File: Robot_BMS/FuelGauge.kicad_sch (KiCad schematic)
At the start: 8 parts, among them IC1 BQ34Z100PWR-R2

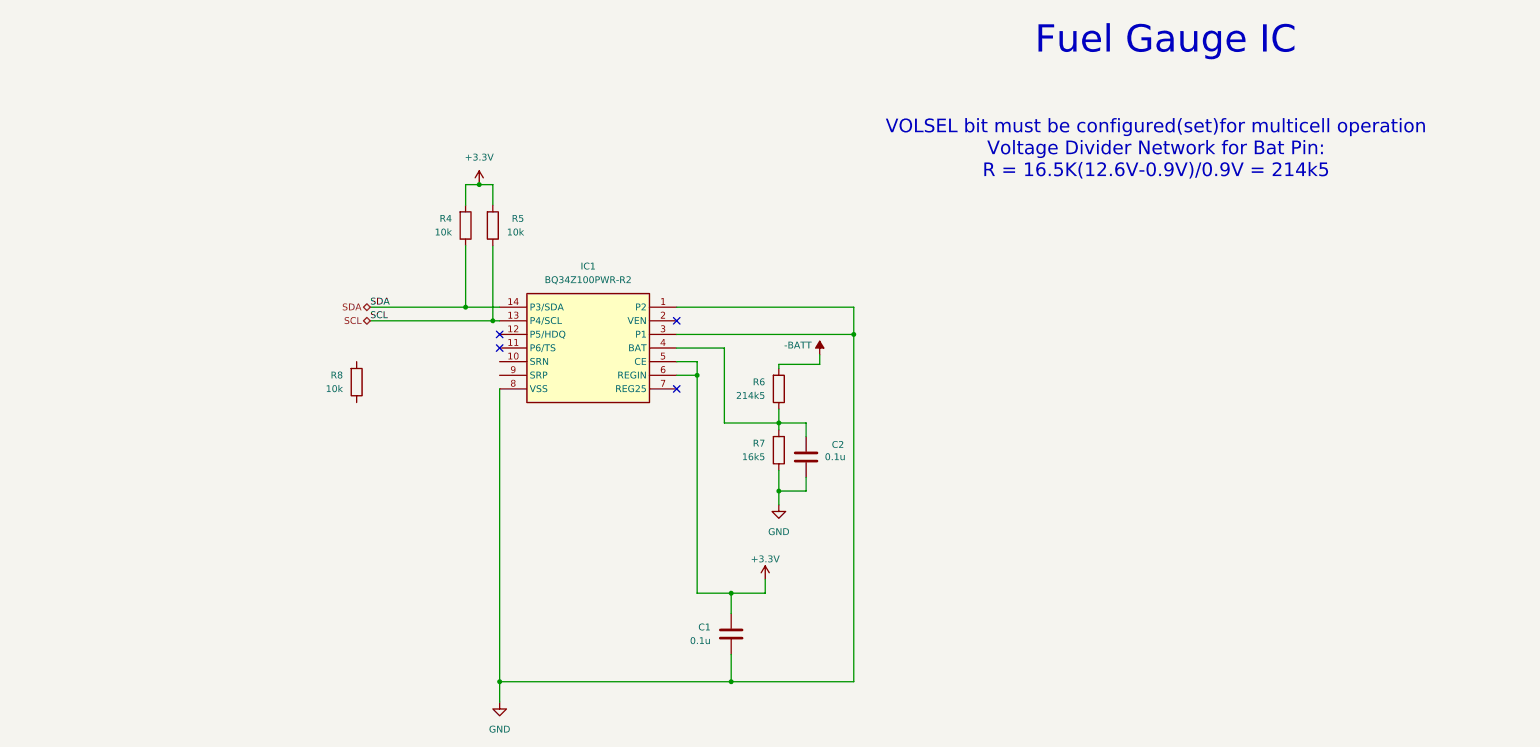
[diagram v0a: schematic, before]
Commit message: DC power supply added via dc Barrel jack
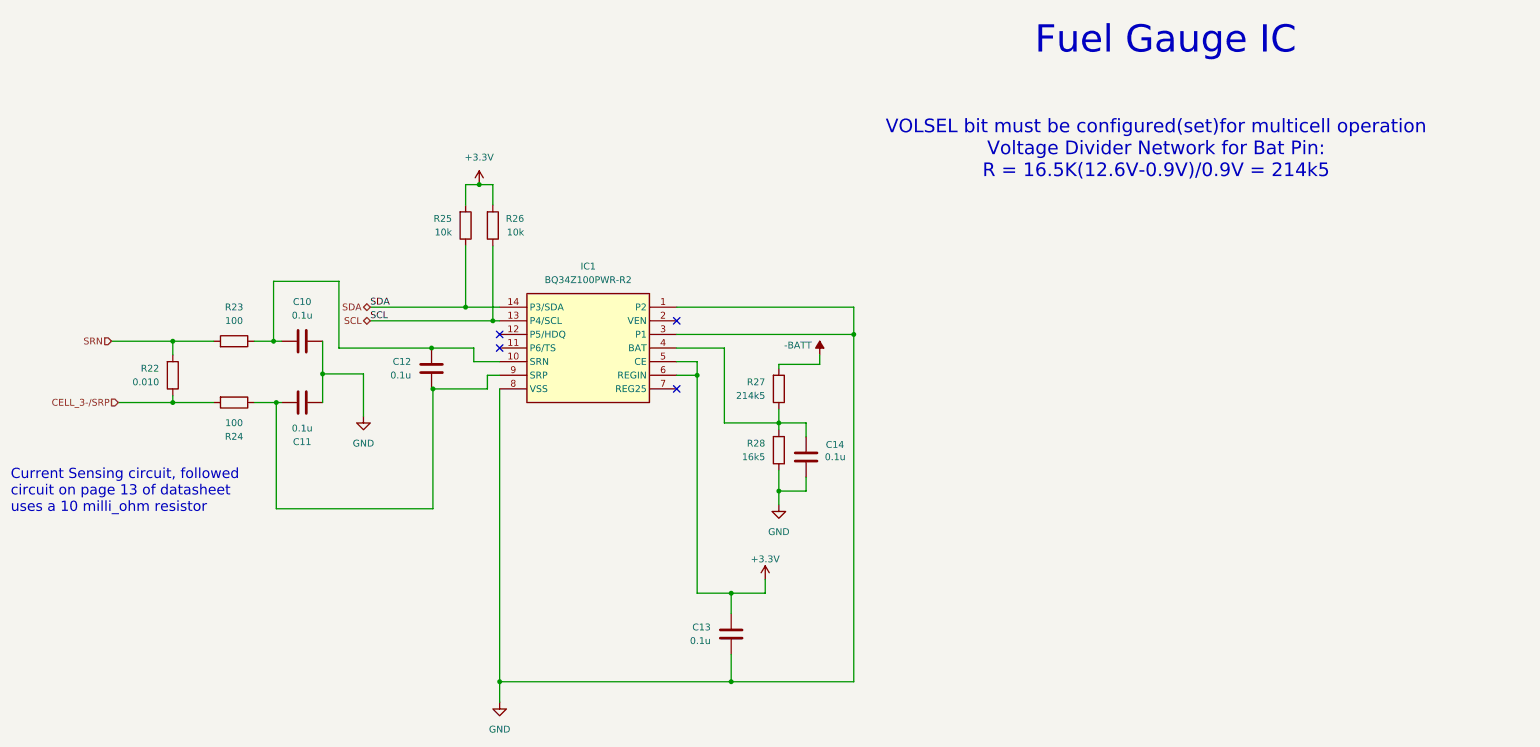
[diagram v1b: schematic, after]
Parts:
- added C10, C11, C12: 0.1u, symbol Device:C
- added R23, R24: 100, symbol Device:R
- R22: renamed from R8; value 10k -> 0.010
- renumbered C1 to C13, C2 to C14, R4 to R25, R5 to R26, R6 to R27, R7 to R28
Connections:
- net GND: now also C10.2, C11.2
- net at IC1.10 (SRN): now also C10.1, C12.1, R23.1
- net at IC1.9 (SRP): now also C11.1, C12.2, R24.1
- net CELL_3-/SRP: now reaches R22.1
- net CELL_3-/SRP: now also R24.2
- net SRN: now reaches R22.2
- net SRN: now also R23.2
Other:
- note added: "Current Sensing circuit, followed circuit on page 13 of datasheet uses a 10 milli_ohm resistor"
- moved on the sheet: R22

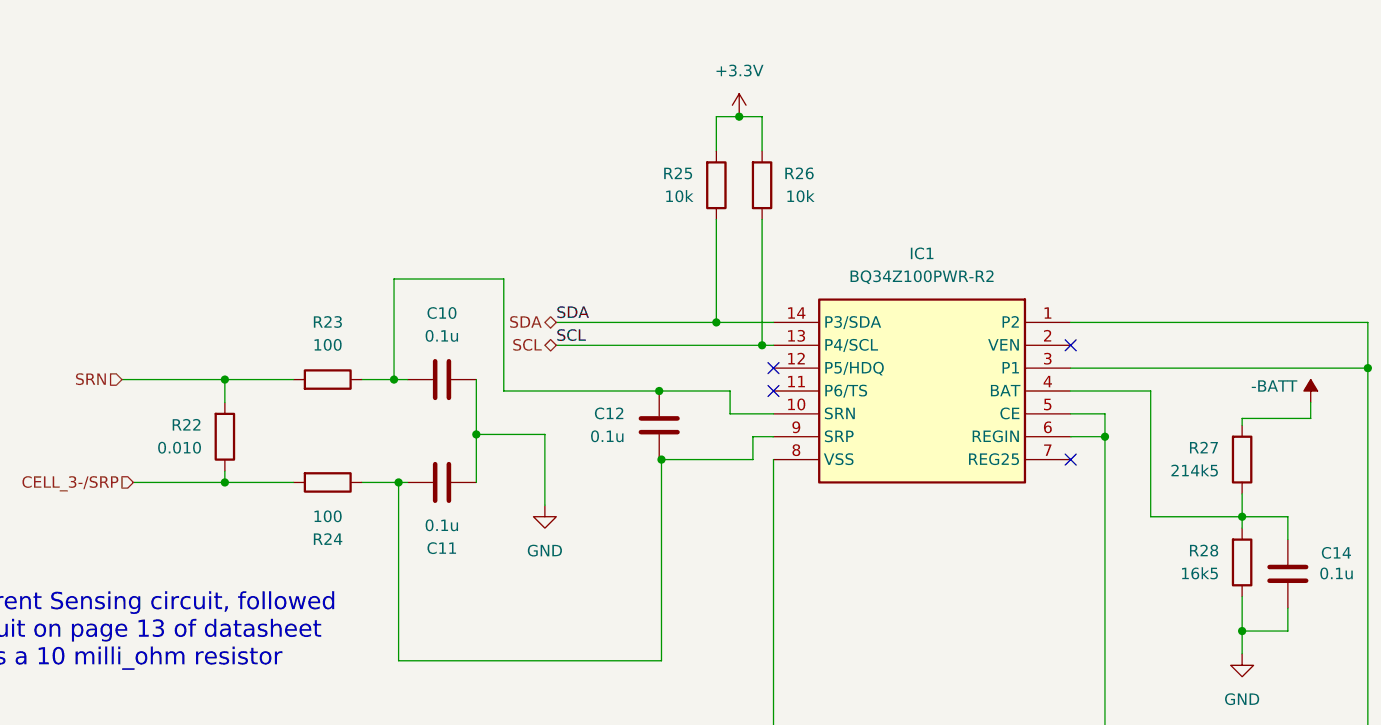
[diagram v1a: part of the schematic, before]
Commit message: implementing sepic converter for Solar power input
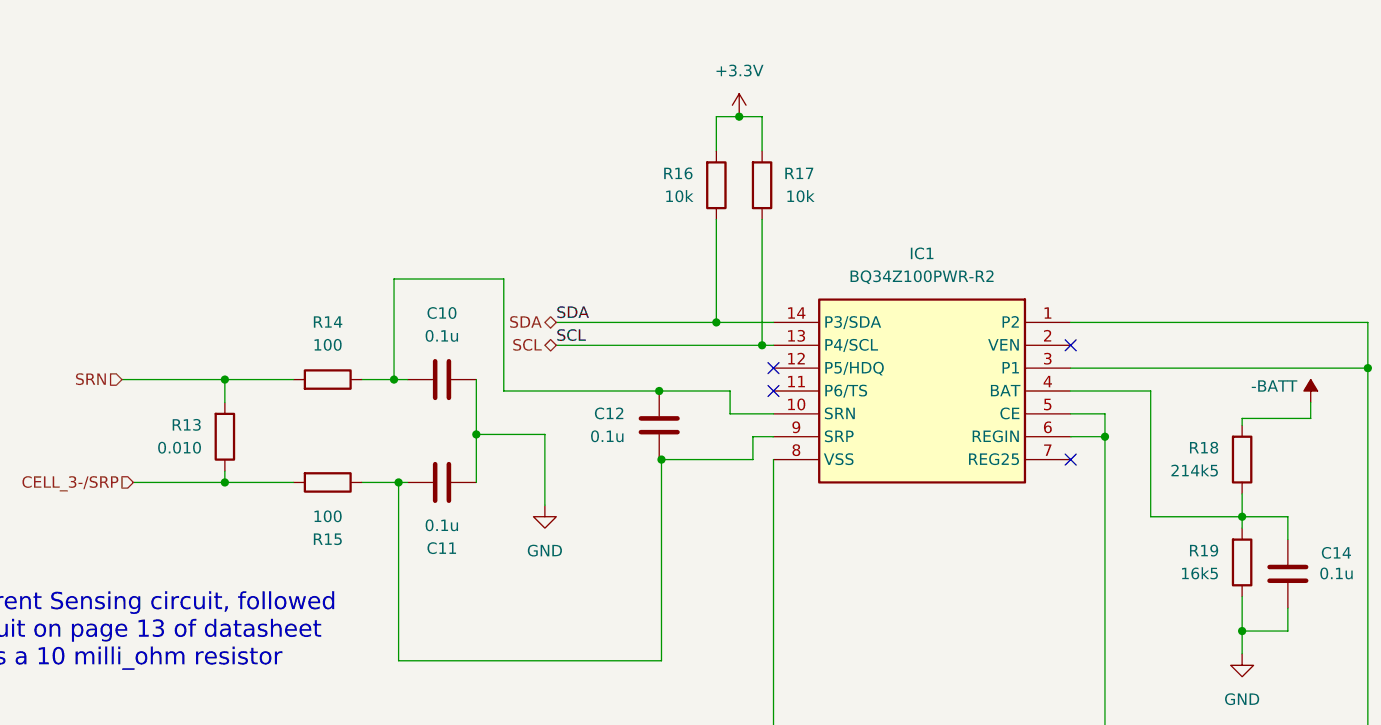
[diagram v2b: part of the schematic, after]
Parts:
- renumbered R22 to R13, R23 to R14, R24 to R15, R25 to R16, R26 to R17, R27 to R18, R28 to R19
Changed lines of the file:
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@@
 		(dnp no)
 		(fields_autoplaced yes)
-		(property "Reference" "R22"
+		(property "Reference" "R13"
 			(at 40.64 86.3599 0)
 			(effects
@@
 			(project "Robot_BMS"
 				(path "/72551b1c-3d40-4199-8911-e5b015f4abec/ddc79d9c-dbaa-4c26-8116-aed3dbdb681b"
-					(reference "R22")
+					(reference "R13")
 					(unit 1)
 				)
@@
 		(on_board yes)
 		(dnp no)
-		(property "Reference" "R26"
+		(property "Reference" "R17"
 			(at 108.712 58.42 0)
 			(effects
@@
 			(project "Robot_BMS"
 				(path "/72551b1c-3d40-4199-8911-e5b015f4abec/ddc79d9c-dbaa-4c26-8116-aed3dbdb681b"
-					(reference "R26")
+					(reference "R17")
 					(unit 1)
 				)
@@
 		(dnp no)
 		(fields_autoplaced yes)
-		(property "Reference" "R23"
+		(property "Reference" "R14"
 			(at 54.61 74.93 90)
 			(effects
@@
 			(project "Robot_BMS"
 				(path "/72551b1c-3d40-4199-8911-e5b015f4abec/ddc79d9c-dbaa-4c26-8116-aed3dbdb681b"
-					(reference "R23")
+					(reference "R14")
 					(unit 1)
 				)
@@
 		(dnp no)
 		(fields_autoplaced yes)
-		(property "Reference" "R27"
+		(property "Reference" "R18"
 			(at 153.67 88.8999 0)
 			(effects
@@
 			(project "Robot_BMS"
 				(path "/72551b1c-3d40-4199-8911-e5b015f4abec/ddc79d9c-dbaa-4c26-8116-aed3dbdb681b"
-					(reference "R27")
+					(reference "R18")
 					(unit 1)
 				)
@@
 		(dnp no)
 		(fields_autoplaced yes)
-		(property "Reference" "R28"
+		(property "Reference" "R19"
 			(at 153.67 100.3299 0)
 			(effects
@@
 			(project "Robot_BMS"
 				(path "/72551b1c-3d40-4199-8911-e5b015f4abec/ddc79d9c-dbaa-4c26-8116-aed3dbdb681b"
-					(reference "R28")
+					(reference "R19")
 					(unit 1)
 				)
@@
 		(on_board yes)
 		(dnp no)
-		(property "Reference" "R24"
+		(property "Reference" "R15"
 			(at 54.61 99.06 90)
 			(effects
@@
 			(project "Robot_BMS"
 				(path "/72551b1c-3d40-4199-8911-e5b015f4abec/ddc79d9c-dbaa-4c26-8116-aed3dbdb681b"
-					(reference "R24")
+					(reference "R15")
 					(unit 1)
 				)
@@
 		(dnp no)
 		(fields_autoplaced yes)
-		(property "Reference" "R25"
+		(property "Reference" "R16"
 			(at 95.25 58.4199 0)
 			(effects
@@
 			(project "Robot_BMS"
 				(path "/72551b1c-3d40-4199-8911-e5b015f4abec/ddc79d9c-dbaa-4c26-8116-aed3dbdb681b"
-					(reference "R25")
-					(unit 1)
-				)
+					(reference "R16")
+					(unit 1)
+				)

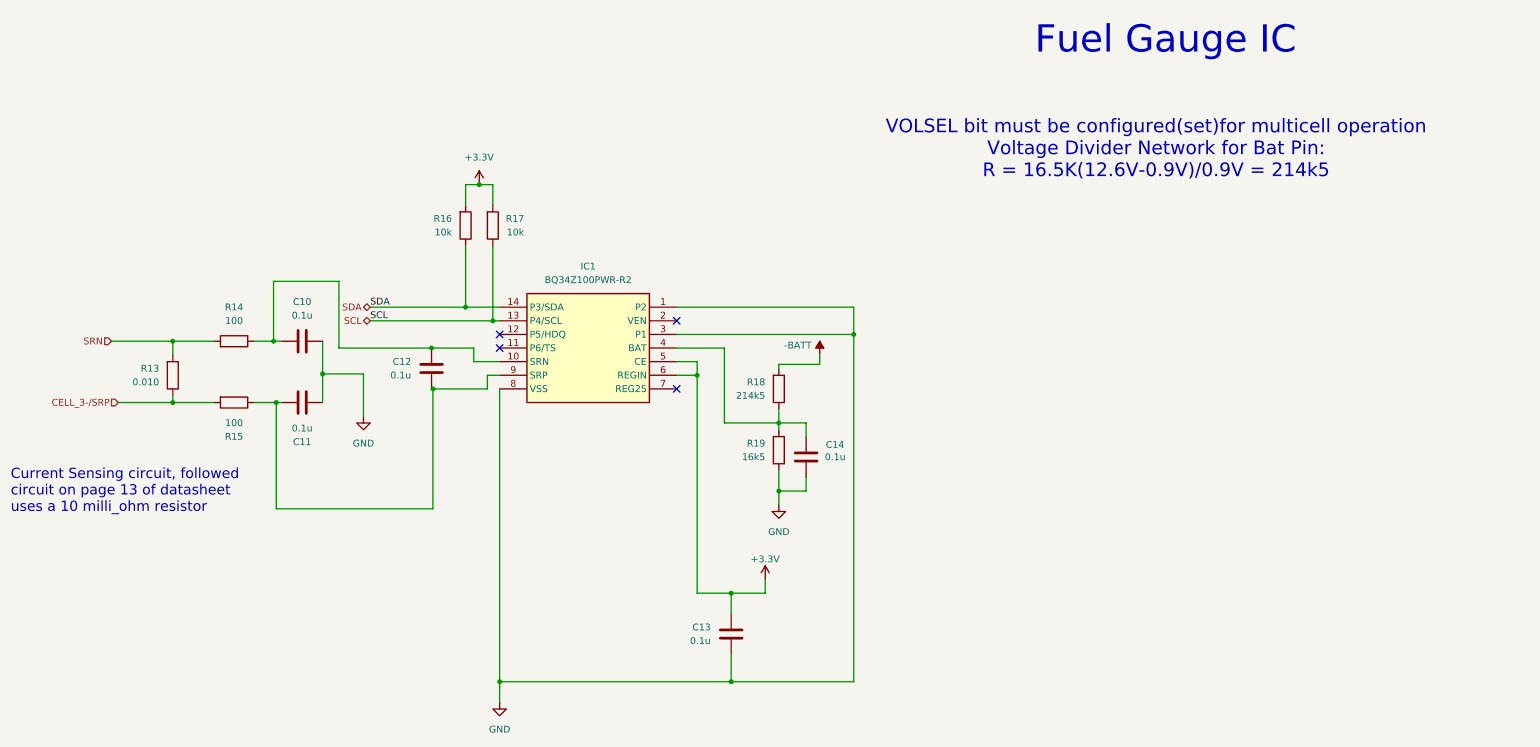
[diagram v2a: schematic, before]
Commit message: solar charger set to 15V
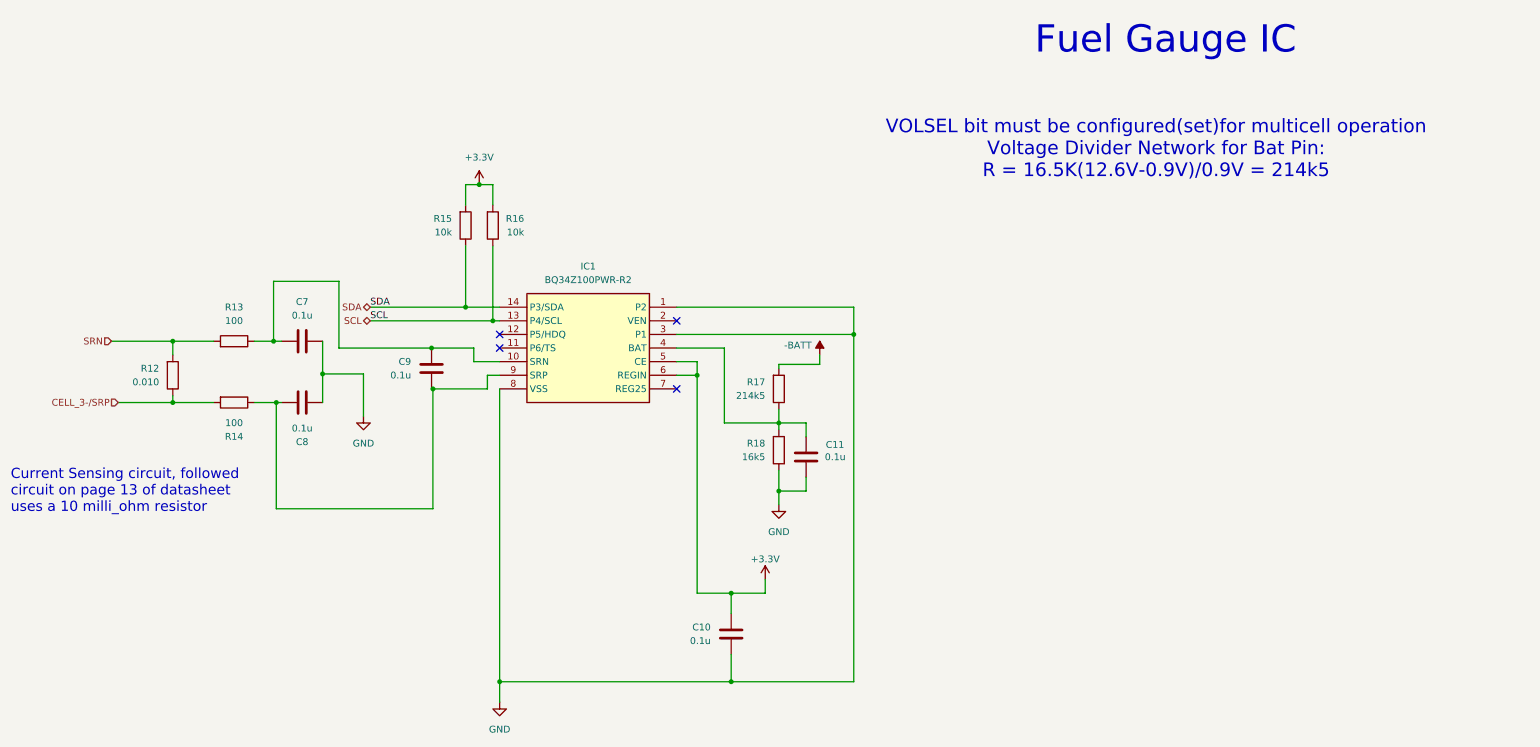
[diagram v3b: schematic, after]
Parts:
- renumbered C13 to C10, C14 to C11, C10 to C7, C11 to C8, C12 to C9, R13 to R12, R14 to R13, R15 to R14, R16 to R15, R17 to R16, R18 to R17, R19 to R18
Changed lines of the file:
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@@
 		(on_board yes)
 		(dnp no)
-		(property "Reference" "#PWR06"
+		(property "Reference" "#PWR010"
 			(at 153.67 129.54 0)
 			(effects
@@
 			(project "Robot_BMS"
 				(path "/72551b1c-3d40-4199-8911-e5b015f4abec/ddc79d9c-dbaa-4c26-8116-aed3dbdb681b"
-					(reference "#PWR06")
+					(reference "#PWR010")
 					(unit 1)
 				)
@@
 		(on_board yes)
 		(dnp no)
-		(property "Reference" "#PWR08"
+		(property "Reference" "#PWR012"
 			(at 163.83 87.63 0)
 			(effects
@@
 			(project "Robot_BMS"
 				(path "/72551b1c-3d40-4199-8911-e5b015f4abec/ddc79d9c-dbaa-4c26-8116-aed3dbdb681b"
-					(reference "#PWR08")
+					(reference "#PWR012")
 					(unit 1)
 				)
@@
 		(dnp no)
 		(fields_autoplaced yes)
-		(property "Reference" "#PWR07"
+		(property "Reference" "#PWR011"
 			(at 156.21 118.11 0)
 			(effects
@@
 			(project "Robot_BMS"
 				(path "/72551b1c-3d40-4199-8911-e5b015f4abec/ddc79d9c-dbaa-4c26-8116-aed3dbdb681b"
-					(reference "#PWR07")
+					(reference "#PWR011")
 					(unit 1)
 				)
@@
 		(dnp no)
 		(fields_autoplaced yes)
-		(property "Reference" "R13"
+		(property "Reference" "R12"
 			(at 40.64 86.3599 0)
 			(effects
@@
 			(project "Robot_BMS"
 				(path "/72551b1c-3d40-4199-8911-e5b015f4abec/ddc79d9c-dbaa-4c26-8116-aed3dbdb681b"
-					(reference "R13")
+					(reference "R12")
 					(unit 1)
 				)
@@
 		(on_board yes)
 		(dnp no)
-		(property "Reference" "R17"
+		(property "Reference" "R16"
 			(at 108.712 58.42 0)
 			(effects
@@
 			(project "Robot_BMS"
 				(path "/72551b1c-3d40-4199-8911-e5b015f4abec/ddc79d9c-dbaa-4c26-8116-aed3dbdb681b"
-					(reference "R17")
+					(reference "R16")
 					(unit 1)
 				)
@@
 		(dnp no)
 		(fields_autoplaced yes)
-		(property "Reference" "#PWR05"
+		(property "Reference" "#PWR09"
 			(at 104.14 154.94 0)
 			(effects
@@
 			(project "Robot_BMS"
 				(path "/72551b1c-3d40-4199-8911-e5b015f4abec/ddc79d9c-dbaa-4c26-8116-aed3dbdb681b"
-					(reference "#PWR05")
+					(reference "#PWR09")
 					(unit 1)
 				)
@@
 		(dnp no)
 		(fields_autoplaced yes)
-		(property "Reference" "C13"
+		(property "Reference" "C10"
 			(at 143.51 134.6199 0)
 			(effects
@@
 			(project "Robot_BMS"
 				(path "/72551b1c-3d40-4199-8911-e5b015f4abec/ddc79d9c-dbaa-4c26-8116-aed3dbdb681b"
-					(reference "C13")
+					(reference "C10")
 					(unit 1)
 				)
@@
 		(dnp no)
 		(fields_autoplaced yes)
-		(property "Reference" "C10"
+		(property "Reference" "C7"
 			(at 67.31 73.9319 90)
 			(effects
@@
 			(project "Robot_BMS"
 				(path "/72551b1c-3d40-4199-8911-e5b015f4abec/ddc79d9c-dbaa-4c26-8116-aed3dbdb681b"
-					(reference "C10")
+					(reference "C7")
 					(unit 1)
 				)
@@
 		(dnp no)
 		(fields_autoplaced yes)
-		(property "Reference" "#PWR04"
+		(property "Reference" "#PWR08"
 			(at 100.33 55.88 0)
 			(effects
@@
 			(project "Robot_BMS"
 				(path "/72551b1c-3d40-4199-8911-e5b015f4abec/ddc79d9c-dbaa-4c26-8116-aed3dbdb681b"
-					(reference "#PWR04")
+					(reference "#PWR08")
 					(unit 1)
 				)
@@
 		(on_board yes)
 		(dnp no)
-		(property "Reference" "C14"
+		(property "Reference" "C11"
 			(at 168.402 100.584 0)
 			(effects
@@
 			(project "Robot_BMS"
 				(path "/72551b1c-3d40-4199-8911-e5b015f4abec/ddc79d9c-dbaa-4c26-8116-aed3dbdb681b"
-					(reference "C14")
+					(reference "C11")
 					(unit 1)
 				)
@@
 		(dnp no)
 		(fields_autoplaced yes)
-		(property "Reference" "#PWR03"
+		(property "Reference" "#PWR07"
 			(at 78.74 101.6 0)
 			(effects
@@
 			(project "Robot_BMS"
 				(path "/72551b1c-3d40-4199-8911-e5b015f4abec/ddc79d9c-dbaa-4c26-8116-aed3dbdb681b"
-					(reference "#PWR03")
+					(reference "#PWR07")
 					(unit 1)
 				)
@@
 		(dnp no)
 		(fields_autoplaced yes)
-		(property "Reference" "R14"
+		(property "Reference" "R13"
 			(at 54.61 74.93 90)
 			(effects
@@
 			(project "Robot_BMS"
 				(path "/72551b1c-3d40-4199-8911-e5b015f4abec/ddc79d9c-dbaa-4c26-8116-aed3dbdb681b"
-					(reference "R14")
+					(reference "R13")
 					(unit 1)
 				)
@@
 		(dnp no)
 		(fields_autoplaced yes)
-		(property "Reference" "R18"
+		(property "Reference" "R17"
 			(at 153.67 88.8999 0)
 			(effects
@@
 			(project "Robot_BMS"
 				(path "/72551b1c-3d40-4199-8911-e5b015f4abec/ddc79d9c-dbaa-4c26-8116-aed3dbdb681b"
-					(reference "R18")
+					(reference "R17")
 					(unit 1)
 				)
@@
 		(dnp no)
 		(fields_autoplaced yes)
-		(property "Reference" "R19"
+		(property "Reference" "R18"
 			(at 153.67 100.3299 0)
 			(effects
@@
 			(project "Robot_BMS"
 				(path "/72551b1c-3d40-4199-8911-e5b015f4abec/ddc79d9c-dbaa-4c26-8116-aed3dbdb681b"
-					(reference "R19")
+					(reference "R18")
 					(unit 1)
 				)
@@
 		(dnp no)
 		(fields_autoplaced yes)
-		(property "Reference" "C12"
+		(property "Reference" "C9"
 			(at 87.63 85.0899 0)
 			(effects
@@
 			(project "Robot_BMS"
 				(path "/72551b1c-3d40-4199-8911-e5b015f4abec/ddc79d9c-dbaa-4c26-8116-aed3dbdb681b"
-					(reference "C12")
+					(reference "C9")
 					(unit 1)
 				)
@@
 		(on_board yes)
 		(dnp no)
-		(property "Reference" "R15"
+		(property "Reference" "R14"
 			(at 54.61 99.06 90)
 			(effects
@@
 			(project "Robot_BMS"
 				(path "/72551b1c-3d40-4199-8911-e5b015f4abec/ddc79d9c-dbaa-4c26-8116-aed3dbdb681b"
-					(reference "R15")
+					(reference "R14")
 					(unit 1)
 				)
@@
 		(dnp no)
 		(fields_autoplaced yes)
-		(property "Reference" "R16"
+		(property "Reference" "R15"
 			(at 95.25 58.4199 0)
 			(effects
@@
 			(project "Robot_BMS"
 				(path "/72551b1c-3d40-4199-8911-e5b015f4abec/ddc79d9c-dbaa-4c26-8116-aed3dbdb681b"
-					(reference "R16")
+					(reference "R15")
 					(unit 1)
 				)
@@
 		(on_board yes)
 		(dnp no)
-		(property "Reference" "C11"
+		(property "Reference" "C8"
 			(at 67.31 100.0581 90)
 			(effects
@@
 			(project "Robot_BMS"
 				(path "/72551b1c-3d40-4199-8911-e5b015f4abec/ddc79d9c-dbaa-4c26-8116-aed3dbdb681b"
-					(reference "C11")
-					(unit 1)
-				)
+					(reference "C8")
+					(unit 1)
+				)
